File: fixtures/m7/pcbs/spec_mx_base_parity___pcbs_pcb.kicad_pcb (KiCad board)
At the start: 2 copper layers, 1 part

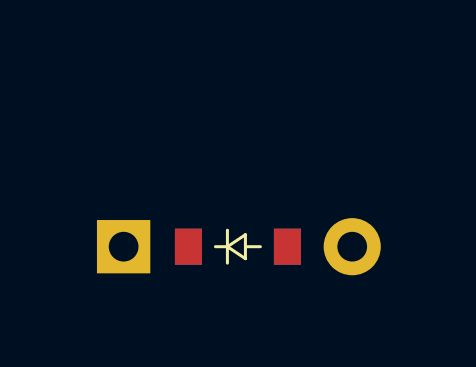
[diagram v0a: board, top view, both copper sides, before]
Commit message: Expand footprint specs and add JS footprints plan
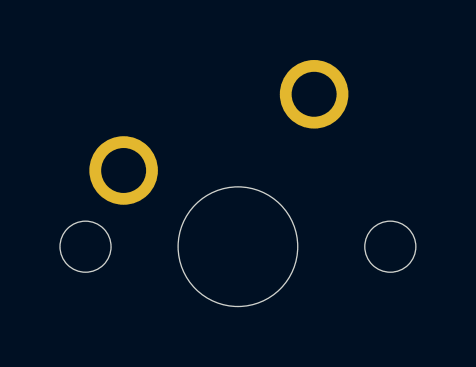
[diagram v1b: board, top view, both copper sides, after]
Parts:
- removed D1: , ComboDiode
- added S1: , MX, F.Cu at (0.00, 0.00)
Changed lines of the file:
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@@
   )
   (net 0 "")
-(net 1 "D_FROM")
-(net 2 "D_TO")
+(net 1 "MX_FROM")
+(net 2 "MX_TO")
   (net_class Default "This is the default net class."
     (clearance 0.2)
@@
     (uvia_drill 0.1)
     (add_net "")
-(add_net "D_FROM")
-(add_net "D_TO")
+(add_net "MX_FROM")
+(add_net "MX_TO")
   )
-        (module ComboDiode (layer F.Cu)
+        (module MX (layer F.Cu)
             (at 0 0 0)
-            (fp_text reference "D1" (at 0 0) (layer F.SilkS) hide (effects (font (size 1.27 1.27) (thickness 0.15))))
+            (fp_text reference "S1" (at 0 0) (layer F.SilkS) hide (effects (font (size 1.27 1.27) (thickness 0.15))))
             (fp_text value "" (at 0 0) (layer F.SilkS) hide (effects (font (size 1.27 1.27) (thickness 0.15))))
-            (fp_line (start 0.25 0) (end 0.75 0) (layer F.SilkS) (width 0.1))
-            (fp_line (start 0.25 0.4) (end -0.35 0) (layer F.SilkS) (width 0.1))
-            (fp_line (start 0.25 -0.4) (end 0.25 0.4) (layer F.SilkS) (width 0.1))
-            (fp_line (start -0.35 0) (end 0.25 -0.4) (layer F.SilkS) (width 0.1))
-            (fp_line (start -0.35 0) (end -0.35 0.55) (layer F.SilkS) (width 0.1))
-            (fp_line (start -0.35 0) (end -0.35 -0.55) (layer F.SilkS) (width 0.1))
-            (fp_line (start -0.75 0) (end -0.35 0) (layer F.SilkS) (width 0.1))
-            (fp_line (start 0.25 0) (end 0.75 0) (layer B.SilkS) (width 0.1))
-            (fp_line (start 0.25 0.4) (end -0.35 0) (layer B.SilkS) (width 0.1))
-            (fp_line (start 0.25 -0.4) (end 0.25 0.4) (layer B.SilkS) (width 0.1))
-            (fp_line (start -0.35 0) (end 0.25 -0.4) (layer B.SilkS) (width 0.1))
-            (fp_line (start -0.35 0) (end -0.35 0.55) (layer B.SilkS) (width 0.1))
-            (fp_line (start -0.35 0) (end -0.35 -0.55) (layer B.SilkS) (width 0.1))
-            (fp_line (start -0.75 0) (end -0.35 0) (layer B.SilkS) (width 0.1))
-            (pad 1 smd rect (at -1.65 0 0) (size 0.9 1.2) (layers F.Cu F.Paste F.Mask) (net 2 "D_TO"))
-            (pad 2 smd rect (at 1.65 0 0) (size 0.9 1.2) (layers B.Cu B.Paste B.Mask) (net 1 "D_FROM"))
-            (pad 1 smd rect (at -1.65 0 0) (size 0.9 1.2) (layers B.Cu B.Paste B.Mask) (net 2 "D_TO"))
-            (pad 2 smd rect (at 1.65 0 0) (size 0.9 1.2) (layers F.Cu F.Paste F.Mask) (net 1 "D_FROM"))
-            (pad 1 thru_hole rect (at -3.81 0 0) (size 1.778 1.778) (drill 0.9906) (layers *.Cu *.Mask) (net 2 "D_TO"))
-            (pad 2 thru_hole circle (at 3.81 0 0) (size 1.905 1.905) (drill 0.9906) (layers *.Cu *.Mask) (net 1 "D_FROM"))
+            (fp_line (start -7 -6) (end -7 -7) (layer Dwgs.User) (width 0.15))
+            (fp_line (start -7 7) (end -6 7) (layer Dwgs.User) (width 0.15))
+            (fp_line (start -6 -7) (end -7 -7) (layer Dwgs.User) (width 0.15))
+            (fp_line (start -7 7) (end -7 6) (layer Dwgs.User) (width 0.15))
+            (fp_line (start 7 6) (end 7 7) (layer Dwgs.User) (width 0.15))
+            (fp_line (start 7 -7) (end 6 -7) (layer Dwgs.User) (width 0.15))
+            (fp_line (start 6 7) (end 7 7) (layer Dwgs.User) (width 0.15))
+            (fp_line (start 7 -7) (end 7 -6) (layer Dwgs.User) (width 0.15))
+            (pad "" np_thru_hole circle (at 0 0) (size 3.9878 3.9878) (drill 3.9878) (layers *.Cu *.Mask))
+            (pad "" np_thru_hole circle (at 5.08 0) (size 1.7018 1.7018) (drill 1.7018) (layers *.Cu *.Mask))
+            (pad "" np_thru_hole circle (at -5.08 0) (size 1.7018 1.7018) (drill 1.7018) (layers *.Cu *.Mask))
+            (pad 1 thru_hole circle (at 2.54 -5.08) (size 2.286 2.286) (drill 1.4986) (layers *.Cu *.Mask) (net 1 "MX_FROM"))
+            (pad 2 thru_hole circle (at -3.81 -2.54) (size 2.286 2.286) (drill 1.4986) (layers *.Cu *.Mask) (net 2 "MX_TO"))
         )
 )
